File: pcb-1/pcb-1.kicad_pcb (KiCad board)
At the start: 2 copper layers, 150 x 100 mm, 6 parts, among them J1 Raspberry_Pi_2_3, J2 Screw_Terminal_01x03, J3 Conn_01x07_Socket, J4 Screw_Terminal_01x02, U1 Pico

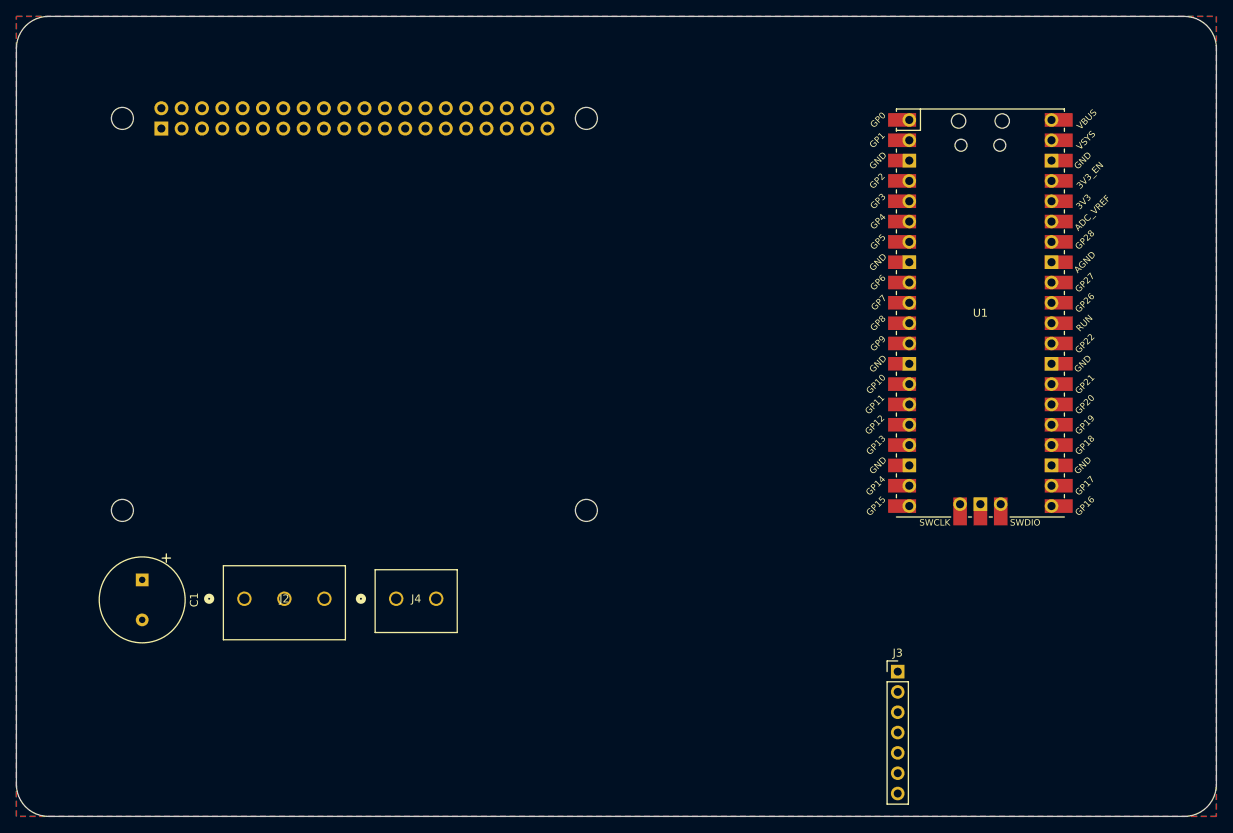
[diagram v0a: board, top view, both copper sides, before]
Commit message: updated directory naming, completed routing? (still unsure about decoupling cap location)
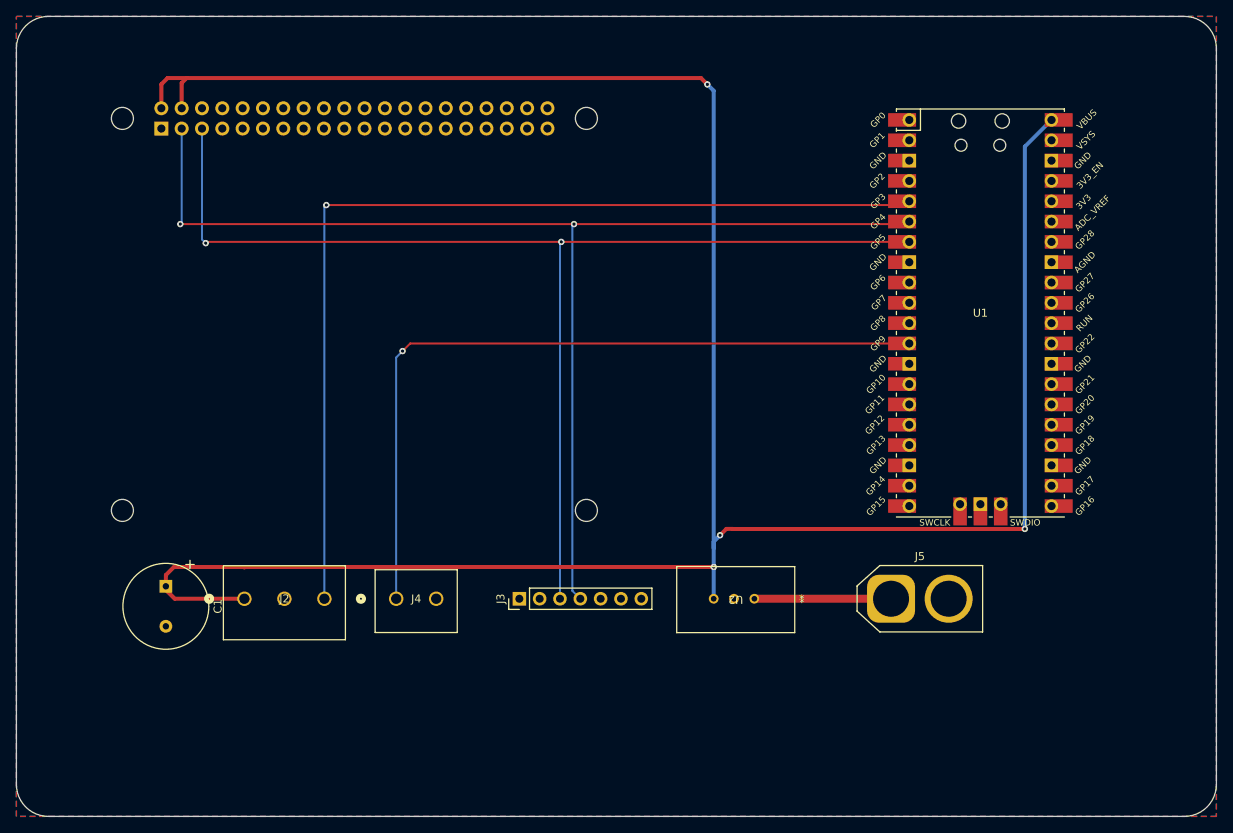
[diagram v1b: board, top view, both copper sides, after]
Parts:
- added J5: Conn_01x02_Socket, Connector_AMASS:AMASS_XT60-F_1x02_P7.20mm_Vertical, F.Cu at (179.3, 127.8)
- added U2: TSR 2-2450, txr:TSR 2-2450_TRP, F.Cu at (162.2, 127.8)
- moved J3 48.2 mm to (132.9, 127.8), turned to 90 degrees
- moved C1 3.07 mm to (88.7, 126.2)
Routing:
- net +5V: track 0.00 -> 314.8 mm, vias 0 -> 4
- net SDA: track 0.00 -> 150.6 mm, vias 0 -> 2
- net SCL: track 0.00 -> 147.2 mm, vias 0 -> 2
- net SERVO: track 0.00 -> 122.4 mm, vias 0 -> 1
- net ESC: track 0.00 -> 95.0 mm, vias 0 -> 1
- net VCC: track 0.00 -> 17.1 mm

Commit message: pcb rerouted with updated trace widths/dimensions
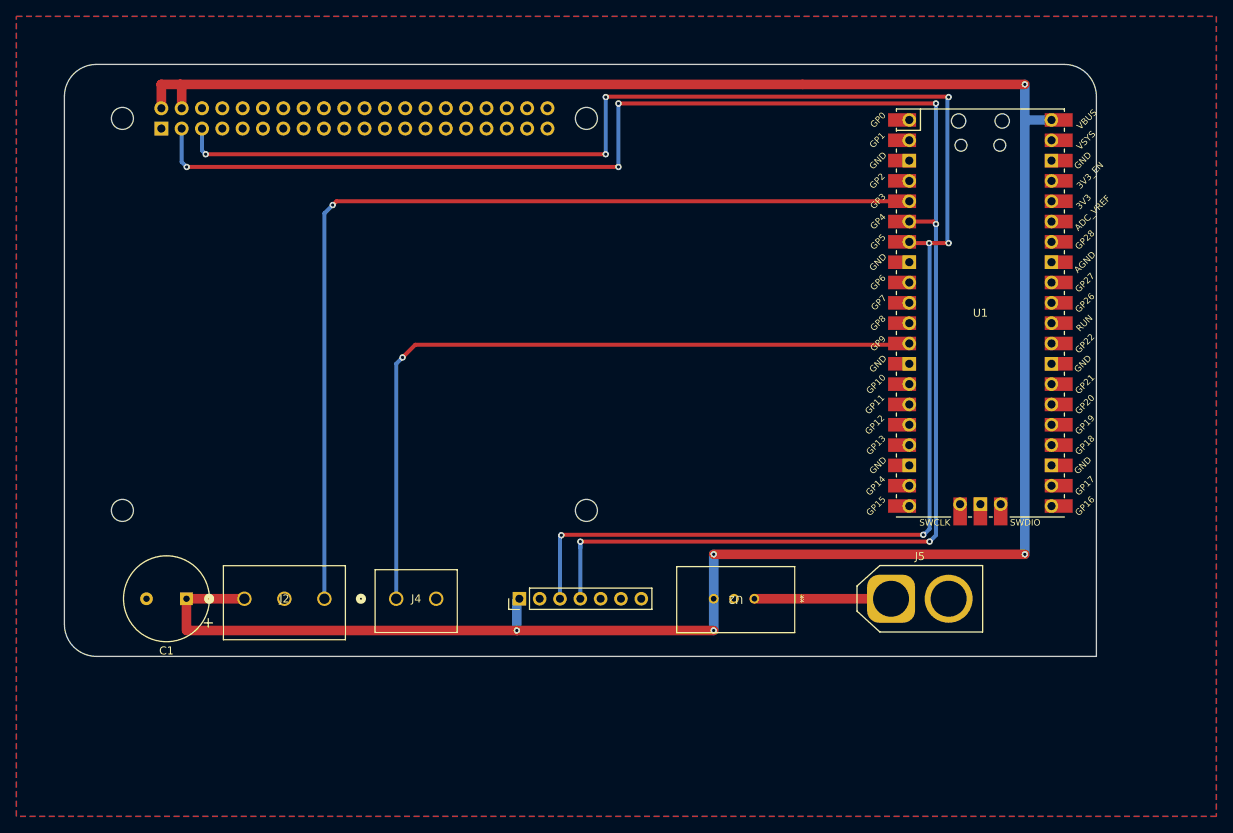
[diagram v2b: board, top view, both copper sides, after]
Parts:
- moved C1 3.01 mm to (91.3, 127.8), turned to 180 degrees
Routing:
- net SCL: track 147.2 -> 216.9 mm, vias 2 -> 8
- net SDA: track 150.6 -> 216.8 mm, vias 2 -> 7
- net +5V: track 314.8 -> 305.8 mm, vias 4 -> 5
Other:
- board size 150 x 100 mm -> 129 x 74 mm

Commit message: removed bad 3v3 net, adjusted dimensions
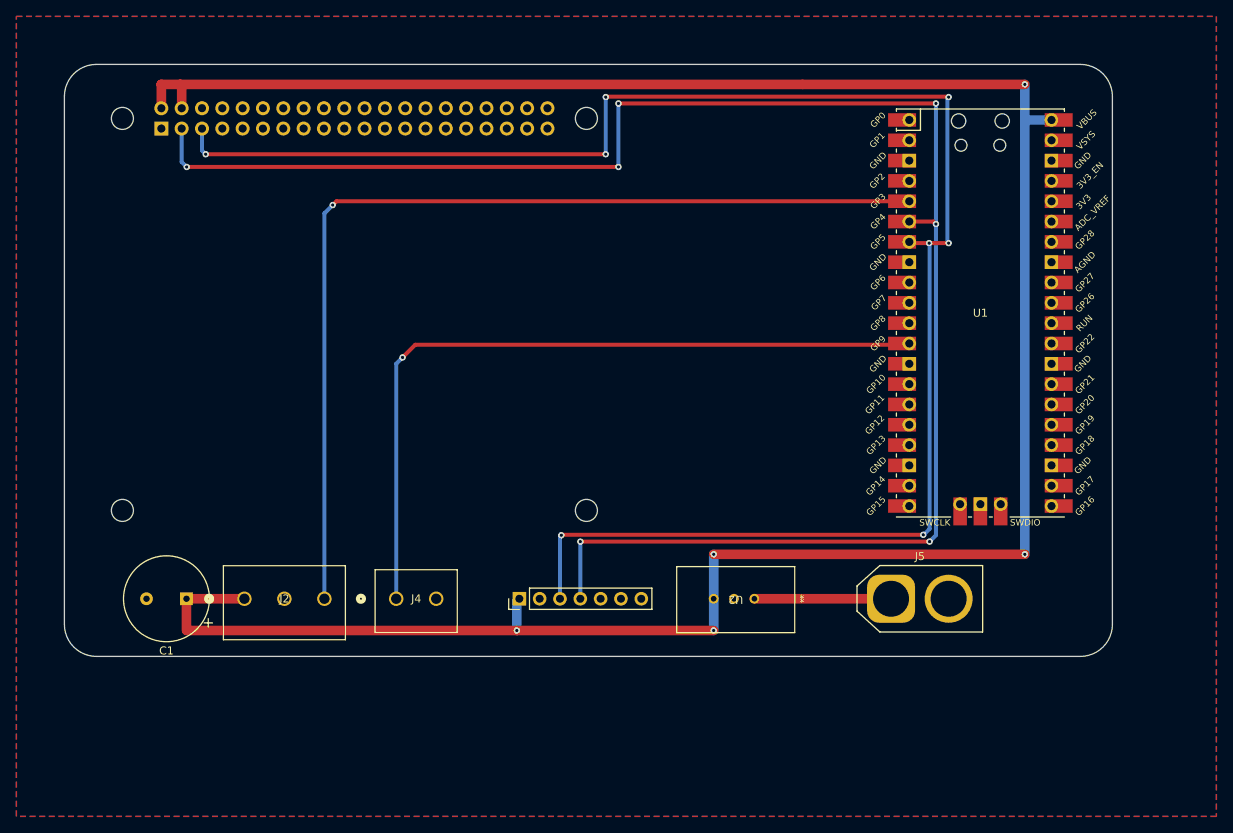
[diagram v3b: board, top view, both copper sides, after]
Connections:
- J1 pad 1: +3V3 -> unconnected-(J1-3V3-Pad1)
- J1 pad 17: +3V3 -> unconnected-(J1-3V3-Pad17)
- U1 pad 36: +3V3 -> unconnected-(U1-3V3-Pad36)
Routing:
- net SDA: track 216.8 -> 216.0 mm
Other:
- board size 129 x 74 mm -> 131 x 74 mm
